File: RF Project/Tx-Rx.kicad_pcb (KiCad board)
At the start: 2 copper layers, 24 parts, among them U1 CC2500RGPR, U2 U.FL_male

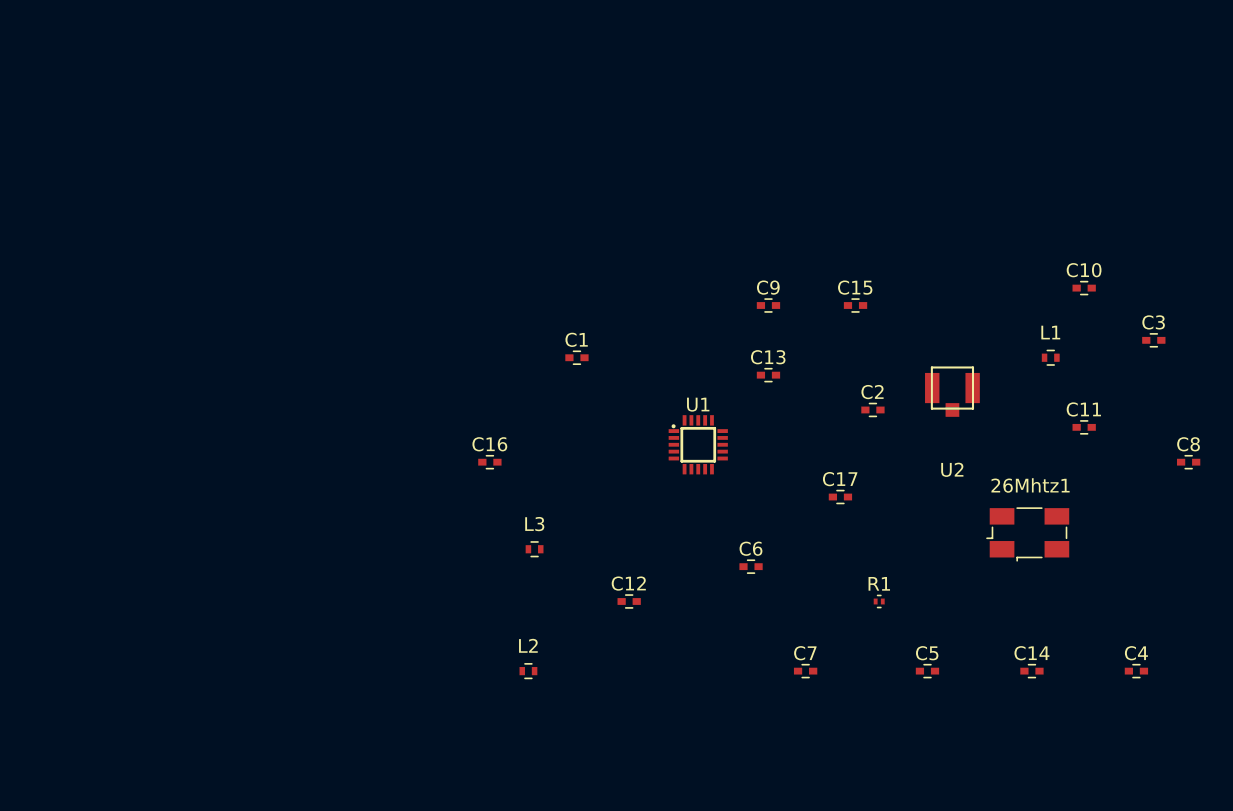
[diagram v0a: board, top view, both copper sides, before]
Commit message: Added Avionics Headers to schematic, fixed library link issues (hopefully) and started working on Layout
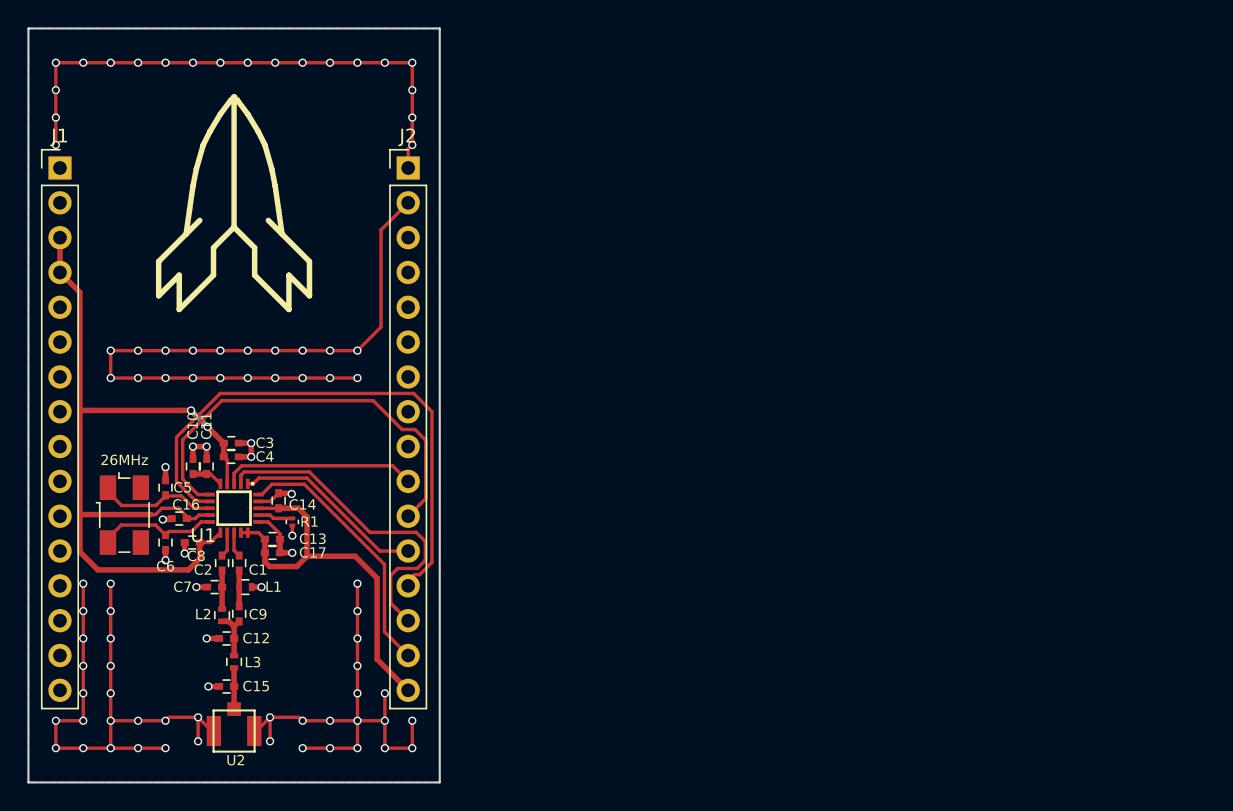
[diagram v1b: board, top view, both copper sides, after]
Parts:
- added J1: CONN_Right, Pin_Headers:Pin_Header_Straight_1x16_Pitch2.54mm, F.Cu at (87.3, 82.7)
- added J2: CONN_Left, Pin_Headers:Pin_Header_Straight_1x16_Pitch2.54mm, F.Cu at (112.7, 82.7)
- moved C8 72.9 mm to (97.0, 110.0), turned to 180 degrees
- moved C4 67.8 mm to (99.8, 103.8)
- moved C3 67.7 mm to (99.8, 102.8)
- moved C10 66.3 mm to (97.0, 104.5), turned to 270 degrees
- moved 26MHz 66.0 mm to (92.0, 108.0), turned to 270 degrees
- moved C11 64.1 mm to (98.0, 104.5), turned to 270 degrees
- moved L1 61.1 mm to (100.8, 113.2)
- moved U2 58.1 mm to (100.0, 123.8), turned to 180 degrees
- moved C5 57.2 mm to (95.0, 106.0), turned to 90 degrees
- moved C14 56.3 mm to (103.2, 107.0), turned to 90 degrees
- moved C15 53.6 mm to (99.5, 120.5), turned to 180 degrees
- moved C2 48.8 mm to (99.1, 111.5), turned to 90 degrees
- moved C9 44.7 mm to (100.4, 115.2), turned to 90 degrees
- moved C7 43.5 mm to (98.6, 113.2), turned to 180 degrees
- moved R1 43.2 mm to (104.2, 108.5), turned to 270 degrees
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- renumbered 26Mhtz1 to 26MHz
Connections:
- U1 pad 1: SCLK -> PD0/SCLK
- U1 pad 2: SO(GDO1) -> PD2/SO(GDO1)
- U1 pad 20: SI -> PD3/SI
- U1 pad 3: GD02 -> PE4/GD02
- U1 pad 6: GDO0 -> PE5/GDO0
- U1 pad 7: CSn -> PD1/CSn
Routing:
- net PWR_GND: track 0.00 -> 190.0 mm, vias 0 -> 95
- net AVDD: track 0.00 -> 89.7 mm, vias 0 -> 2
- net PD1/CSn: track 0.00 -> 40.4 mm
- net PE5/GDO0: track 0.00 -> 32.0 mm
- net PD2/SO(GDO1): track 0.00 -> 24.5 mm
- net PD3/SI: track 0.00 -> 19.3 mm
- net PD0/SCLK: track 0.00 -> 14.6 mm
- net PE4/GD02: track 0.00 -> 14.2 mm
- net XOSC_Q1: track 0.00 -> 8.87 mm
- net XOSC_Q2: track 0.00 -> 8.82 mm
- net Net-(C12-Pad1): track 0.00 -> 3.69 mm
- net Net-(C15-Pad1): track 0.00 -> 3.00 mm
- net Net-(C2-Pad1): track 0.00 -> 2.80 mm
- net Net-(C1-Pad2): track 0.00 -> 2.60 mm
- net Net-(R1-Pad1): track 0.00 -> 2.60 mm
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- added copper zone on B.Cu, net PWR_GND
- added copper zone on F.Cu, net PWR_GND
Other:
- board outline added: 30 x 55 mm

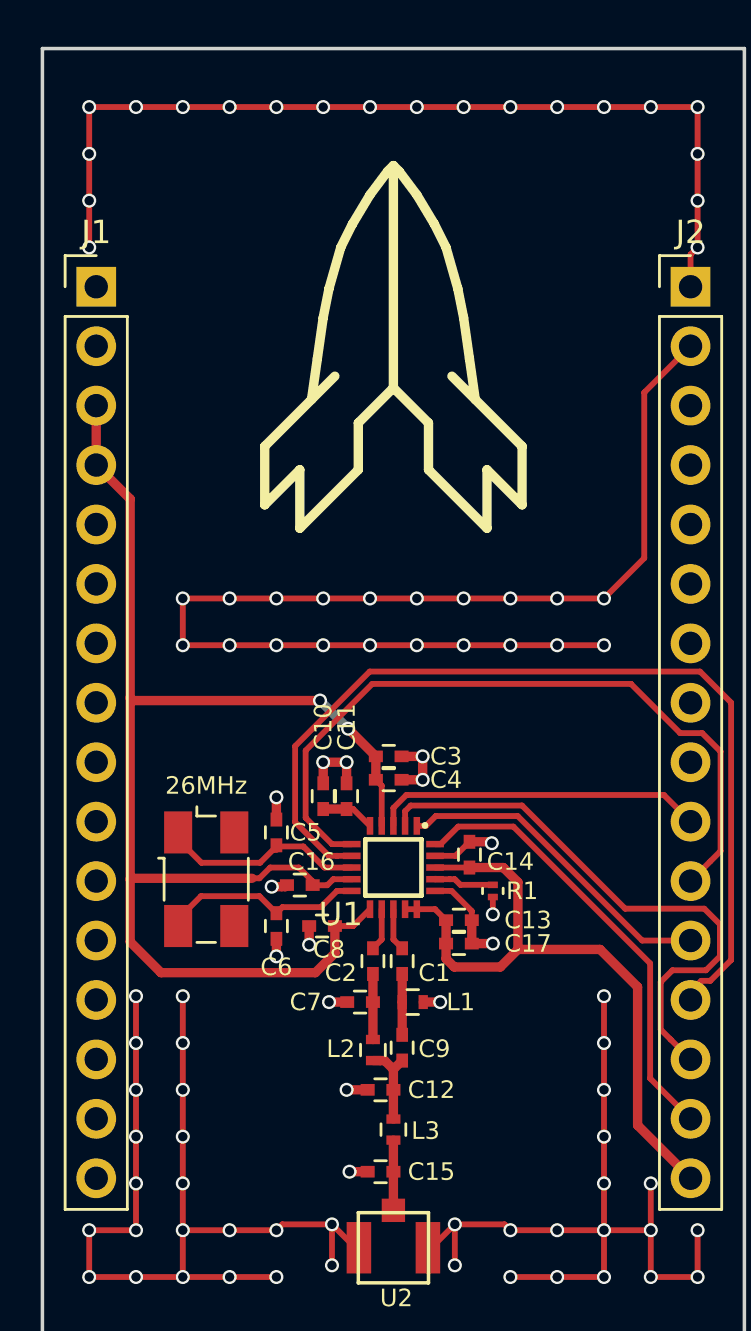
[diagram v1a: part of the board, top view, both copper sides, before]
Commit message: Fixed CC2500 footprint (missing gnd pad) finished layout, needs CDR
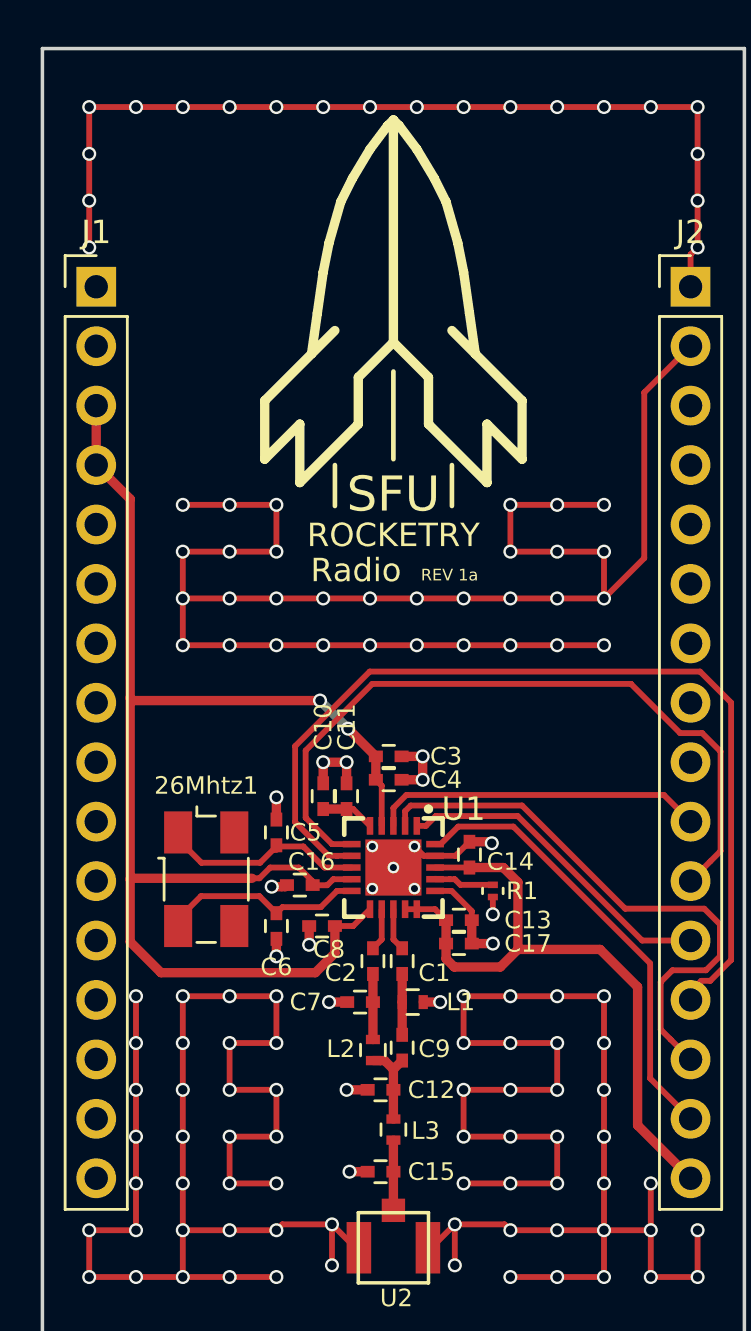
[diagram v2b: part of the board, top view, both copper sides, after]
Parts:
- renumbered 26MHz to 26Mhtz1
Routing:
- net PWR_GND: track 190.0 -> 273.5 mm, vias 95 -> 137
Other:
- board text added: "REV 1a"
- board text added: "ROCKETRY"
- board text added: "Radio"
- board text added: "SFU"

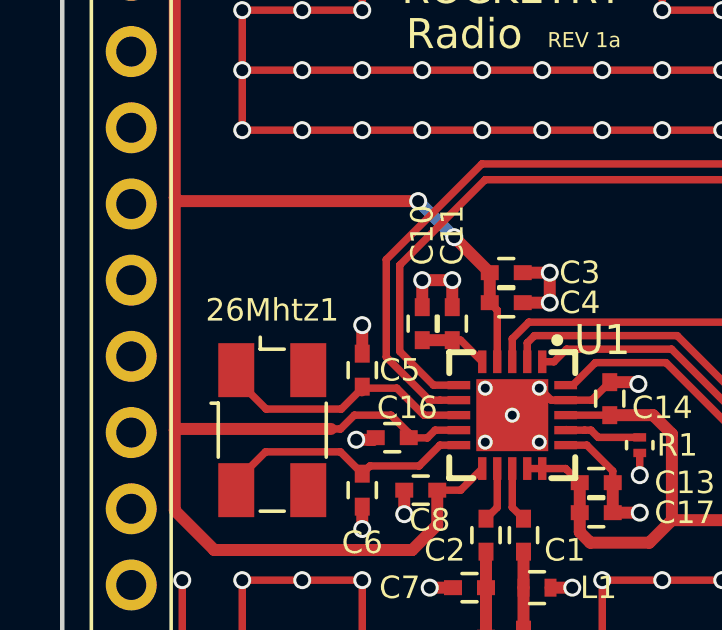
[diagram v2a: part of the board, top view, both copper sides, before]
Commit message: fixed Crystal SilkScreen label
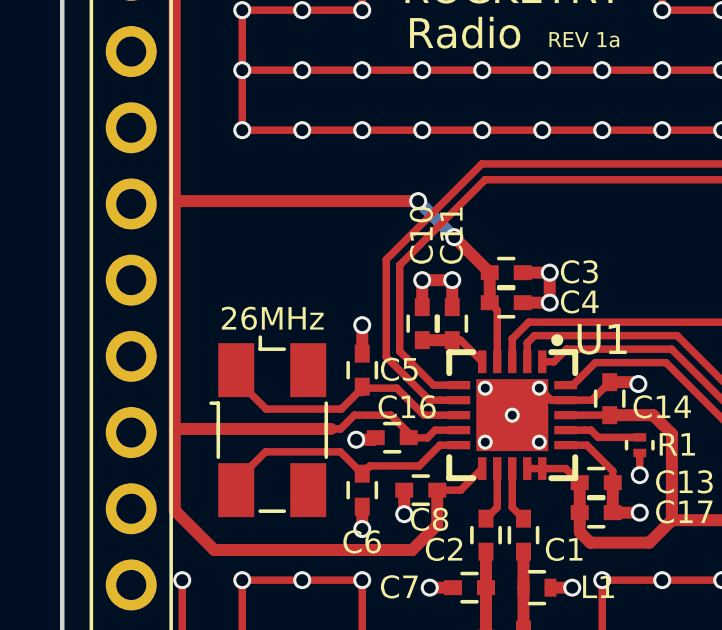
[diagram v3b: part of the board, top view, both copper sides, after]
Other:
- board text added: "26MHz"
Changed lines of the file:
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@@
     (area 84.924999 72.424999 115.075001 127.575001)
     (thickness 1.6)
-    (drawings 92)
+    (drawings 93)
     (tracks 440)
     (zones 0)
@@
     (tags "SMD SMT crystal")
     (attr smd)
-    (fp_text reference 26Mhtz1 (at -4 0 360) (layer F.SilkS)
+    (fp_text reference 26Mhtz1 (at -4 0 360) (layer F.SilkS) hide
       (effects (font (size 0.75 0.75) (thickness 0.15)))
     )
@@
       (net 8 PWR_GND))
   )
+  (gr_text 26MHz (at 92 104.3) (layer F.SilkS)
+    (effects (font (size 0.75 0.75) (thickness 0.1875)))
+  )
   (gr_text "REV 1a" (at 100 126.7 360) (layer B.SilkS)

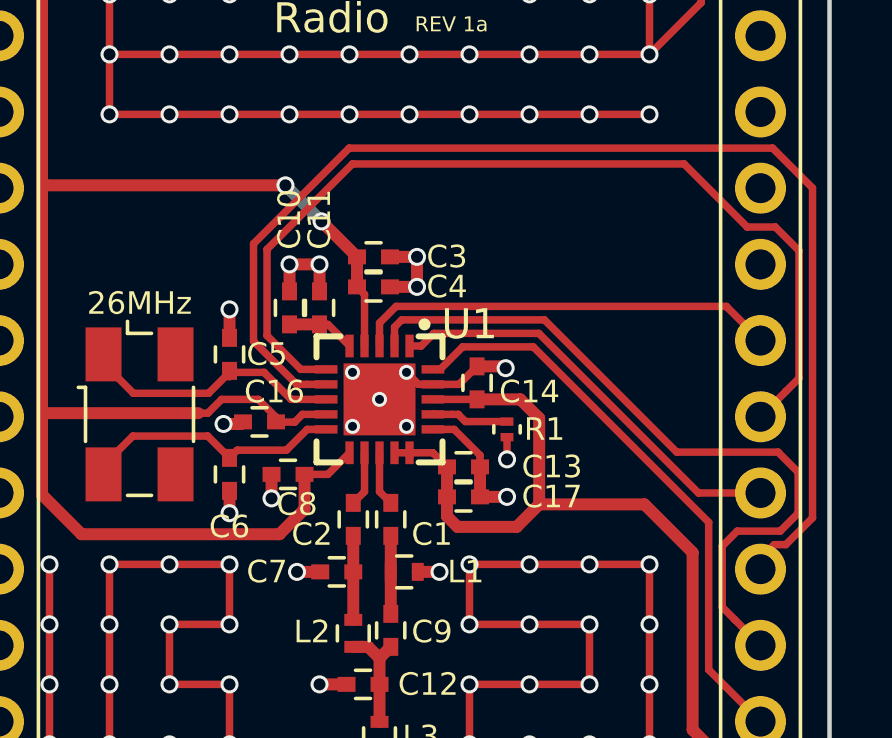
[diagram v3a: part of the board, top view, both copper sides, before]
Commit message: Moved components so that they weren't inside the CC2500 (woops), also changed the resistor to 0402 instead of 0201 since those aren't in stock QQ
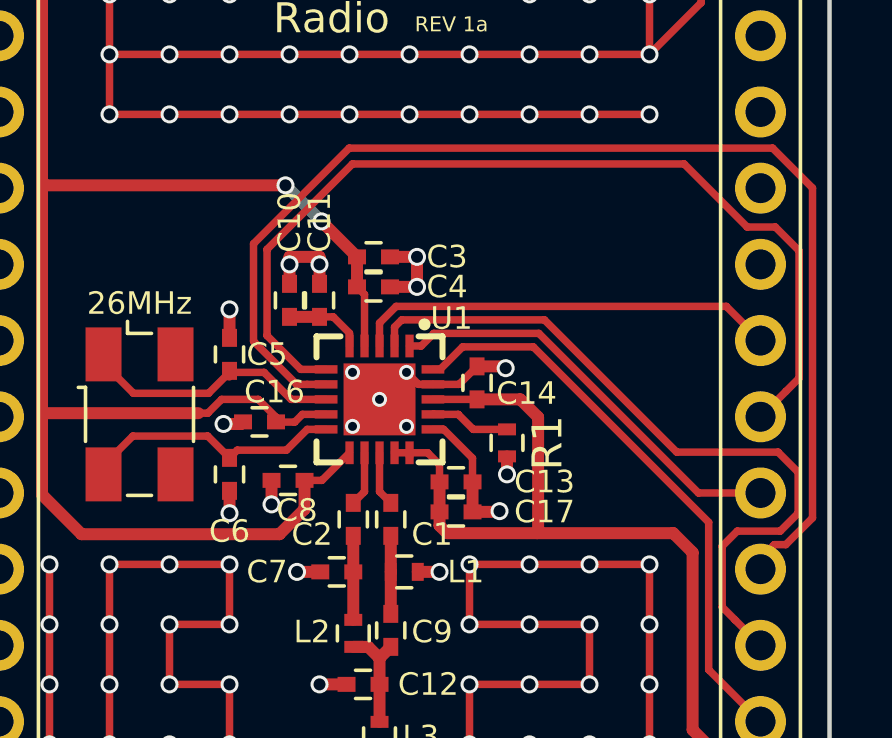
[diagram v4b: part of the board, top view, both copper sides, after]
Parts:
- C14, C16, C17: value 220μF -> 220pF
- R1: footprint Resistors_SMD:R_0201 -> Resistors_SMD:R_0402
- moved C13 0.56 mm to (102.5, 110.2)
- moved C17 0.56 mm to (102.5, 111.2)
- moved R1 0.45 mm to (104.2, 109.0)
- moved C10 0.25 mm to (97.0, 104.2)
- moved C11 0.25 mm to (98.0, 104.2)
- moved C8 0.20 mm to (97.0, 110.2)

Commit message: Fixed my poor attempt to move stuff :(
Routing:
- net PWR_GND: track 273.5 -> 273.0 mm
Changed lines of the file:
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@@
   (segment (start 99.25 103.75) (end 99.5 104) (width 0.25) (layer F.Cu) (net 7))
   (segment (start 99.5 104) (end 99.5 105.72) (width 0.25) (layer F.Cu) (net 7))
+  (segment (start 98 103) (end 98 103.65) (width 0.4) (layer F.Cu) (net 8))
+  (segment (start 97 103) (end 98 103) (width 0.4) (layer F.Cu) (net 8))
+  (via (at 98 103) (size 0.6) (drill 0.4) (layers F.Cu B.Cu) (net 8))
+  (segment (start 97 103.65) (end 97 103) (width 0.4) (layer F.Cu) (net 8))
+  (via (at 97 103) (size 0.6) (drill 0.4) (layers F.Cu B.Cu) (net 8))
   (segment (start 96.4 110.2) (end 96.4 111) (width 0.4) (layer F.Cu) (net 8))
   (via (at 96.4 111) (size 0.6) (drill 0.4) (layers F.Cu B.Cu) (net 8))
@@
   (segment (start 95 105.45) (end 95 104.5) (width 0.4) (layer F.Cu) (net 8))
   (via (at 95 104.5) (size 0.6) (drill 0.4) (layers F.Cu B.Cu) (net 8))
-  (segment (start 98 102.75) (end 98 103.65) (width 0.4) (layer F.Cu) (net 8))
-  (segment (start 97 102.75) (end 98 102.75) (width 0.4) (layer F.Cu) (net 8))
-  (segment (start 97 103.65) (end 97 102.75) (width 0.4) (layer F.Cu) (net 8))
   (via (at 98.125 120.5) (size 0.6) (drill 0.4) (layers F.Cu B.Cu) (net 8))
   (segment (start 98.9 117) (end 98.125 117) (width 0.25) (layer F.Cu) (net 8))
@@
   (segment (start 101.775 123.6) (end 102.625 122.75) (width 0.25) (layer F.Cu) (net 8))
   (via (at 102.625 122.75) (size 0.6) (drill 0.4) (layers F.Cu B.Cu) (net 8))
-  (via (at 98 103) (size 0.6) (drill 0.4) (layers F.Cu B.Cu) (net 8))
-  (via (at 97 103) (size 0.6) (drill 0.4) (layers F.Cu B.Cu) (net 8))
   (segment (start 99.125 115.75) (end 99.441876 115.75) (width 0.4) (layer F.Cu) (net 9))
   (segment (start 99.441876 115.75) (end 99.44203 115.750154) (width 0.4) (layer F.Cu) (net 9))

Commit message: Labelled headers Left/Right since someone who isn't me totally messed up and put the right header on the left and the left header on the right then did the entire layout and doesn't want to redo it (sounds like a rev 2 :p)
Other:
- board text added: "L"
- board text added: "R"
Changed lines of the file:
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@@
     (area 84.924999 72.424999 115.075001 127.575001)
     (thickness 1.6)
-    (drawings 93)
+    (drawings 97)
     (tracks 442)
     (zones 0)
@@
   )
   (setup
-    (last_trace_width 0.4)
+    (last_trace_width 0.25)
     (user_trace_width 0.4)
     (trace_clearance 0.2)
@@
       (rotate (xyz 0 0 0))
     )
+  )
+  (gr_text L (at 110 82.5) (layer B.SilkS)
+    (effects (font (size 1.5 1.5) (thickness 0.3)) (justify mirror))
+  )
+  (gr_text R (at 90 82.5) (layer B.SilkS)
+    (effects (font (size 1.5 1.5) (thickness 0.3)) (justify mirror))
+  )
+  (gr_text R (at 90 82.5) (layer F.SilkS)
+    (effects (font (size 1.5 1.5) (thickness 0.3)))
+  )
+  (gr_text L (at 110 82.5) (layer F.SilkS)
+    (effects (font (size 1.5 1.5) (thickness 0.3)))
   )
   (gr_text 26MHz (at 92 104.3) (layer F.SilkS)
@@
     )
   )
+  (zone (net 0) (net_name "") (layer B.Mask) (hatch edge 0.508)
+    (connect_pads (clearance 0.2))
+    (min_thickness 0.254)
+    (fill yes (arc_segments 16) (thermal_gap 0.508) (thermal_bridge_width 0.508))
+    (polygon
+      (pts
+        (xy 100.2 76.06) (xy 100.2 84.97) (xy 101.63 86.4) (xy 101.66 86.43) (xy 101.68 86.46)
+        (xy 101.69 86.49) (xy 101.7 86.53) (xy 101.7 88.47) (xy 103.8 90.57) (xy 103.8 88.54)
+        (xy 103.81 88.49) (xy 103.84 88.43) (xy 103.87 88.4) (xy 103.9 88.38) (xy 103.94 88.36)
+        (xy 104 88.35) (xy 104.06 88.36) (xy 104.1 88.38) (xy 104.13 88.4) (xy 105.3 89.57)
+        (xy 105.3 87.63) (xy 102.36 84.69) (xy 102.3 84.57) (xy 102.33 84.45) (xy 102.4 84.38)
+        (xy 102.52 84.35) (xy 102.65 84.42) (xy 103.22 84.99) (xy 103.05 83.8) (xy 102.8 82.08)
+        (xy 102.55 80.82) (xy 102.06 79.11) (xy 101.58 78.15) (xy 100.84 76.92)
+      )
+    )
+  )
   (zone (net 0) (net_name "") (layer F.Mask) (hatch edge 0.508)
     (priority 15)
@@
       )
     )
+  )
+  (zone (net 0) (net_name "") (layer B.Mask) (hatch edge 0.508)
+    (connect_pads (clearance 0.2))
+    (min_thickness 0.254)
+    (fill yes (arc_segments 16) (thermal_gap 0.508) (thermal_bridge_width 0.508))
+    (polygon
+      (pts
+        (xy 99.8 76.06) (xy 99.16 76.92) (xy 98.42 78.15) (xy 97.94 79.11) (xy 97.45 80.82)
+        (xy 97.2 82.08) (xy 96.95 83.8) (xy 96.78 84.99) (xy 97.35 84.42) (xy 97.48 84.35)
+        (xy 97.6 84.38) (xy 97.67 84.45) (xy 97.7 84.57) (xy 97.64 84.69) (xy 96.625 85.7)
+        (xy 94.7 87.63) (xy 94.7 89.57) (xy 95.87 88.4) (xy 95.9 88.38) (xy 95.94 88.36)
+        (xy 96 88.35) (xy 96.06 88.36) (xy 96.1 88.38) (xy 96.13 88.4) (xy 96.16 88.43)
+        (xy 96.19 88.49) (xy 96.2 88.54) (xy 96.2 90.57) (xy 98.3 88.47) (xy 98.3 86.53)
+        (xy 98.31 86.49) (xy 98.32 86.46) (xy 98.34 86.43) (xy 98.37 86.4) (xy 99.8 84.97)
+      )
+    )
